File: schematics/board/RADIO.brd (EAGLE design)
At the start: 29 x 49 mm, 2 parts

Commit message: Платы подготовлены для Резонита
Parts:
- moved JP1 1.12 mm to (12.3, 47.5)
- moved RADIO 1.00 mm to (27.0, 5.23)
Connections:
- net N$1 renamed GND
- net N$2 renamed 5V
- net N$3 renamed AUX
- net N$4 renamed TXD
- net N$5 renamed RXD
- net N$6 renamed M1
- net N$7 renamed M0
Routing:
- net GND: track 79.7 -> 89.7 mm, vias 1 -> 0
- net RXD: track 22.8 -> 21.7 mm
- net M1: track 26.4 -> 25.3 mm
- net TXD: track 19.1 -> 18.1 mm
- net 5V: track 11.9 -> 10.9 mm
- net AUX: track 15.5 -> 14.5 mm
- net M0: track 29.8 -> 28.9 mm
- added copper zone on layer 1, net GND
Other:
- board size 29 x 49 mm -> 29 x 51 mm
- board text added: "5V"
- board text added: "AUX"
- board text added: "GND"
- board text added: "M0"
- board text added: "M1"
- board text added: "RX"
- board text added: "TX"

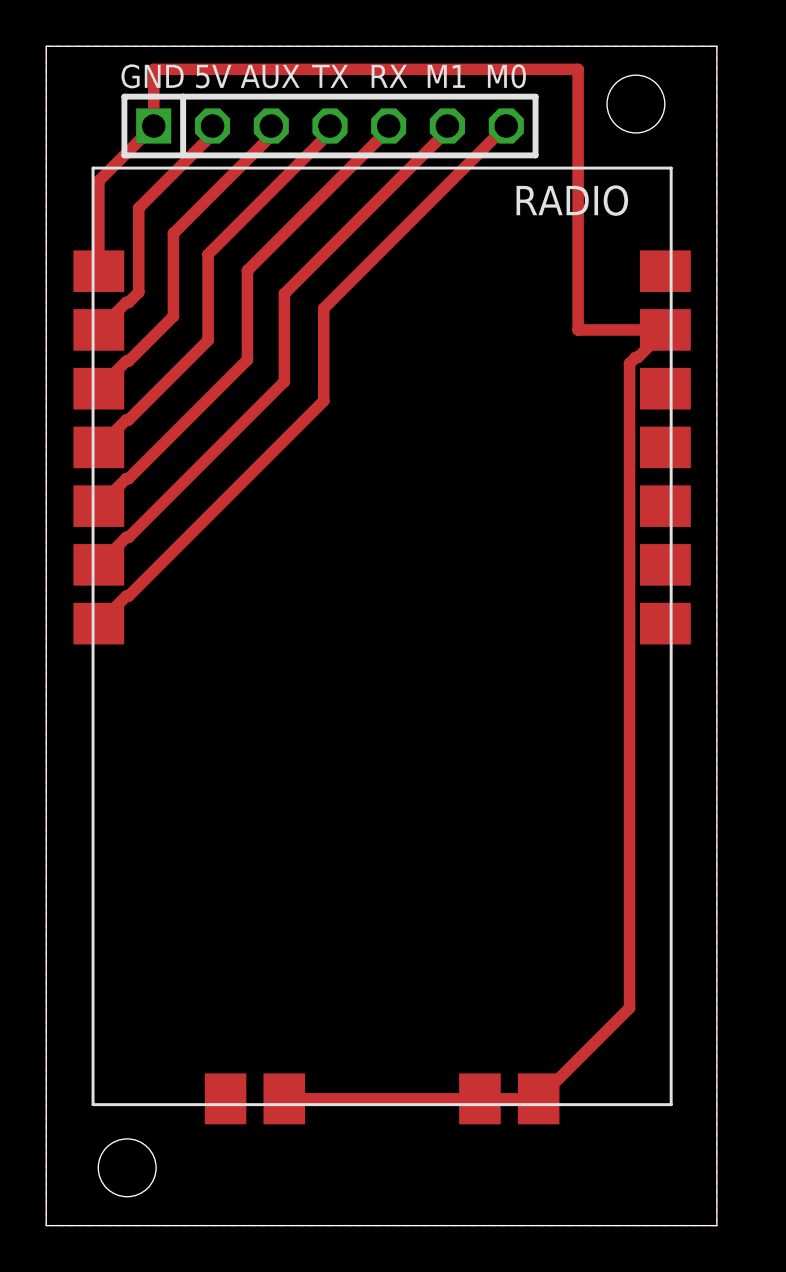
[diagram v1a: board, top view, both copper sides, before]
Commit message: GKS: допиливается конструкция, изменены размеры платы под радио
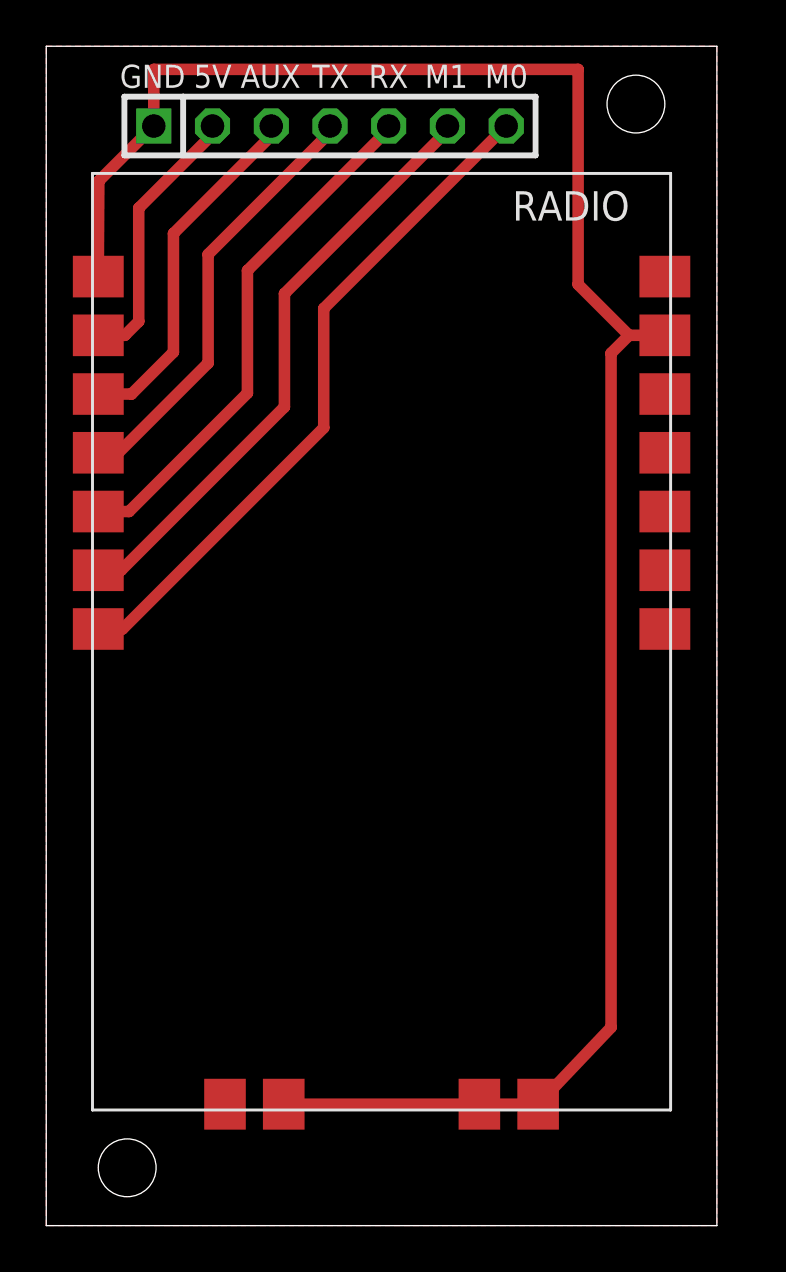
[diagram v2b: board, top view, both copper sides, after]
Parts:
- moved RADIO 0.23 mm to (27.0, 5.00)
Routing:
- net GND: track 89.7 -> 88.1 mm
- net AUX: track 14.5 -> 15.5 mm
- net RXD: track 21.7 -> 22.7 mm
- net 5V: track 10.9 -> 11.8 mm
- net M0: track 28.9 -> 29.7 mm
- net M1: track 25.3 -> 26.0 mm
- net TXD: track 18.1 -> 18.8 mm
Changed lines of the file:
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@@
 <?xml version="1.0" encoding="utf-8"?>
 <!DOCTYPE eagle SYSTEM "eagle.dtd">
-<eagle version="9.4.2">
+<eagle version="9.6.0">
 <drawing>
 <settings>
@@
 <attribute name="VALUE" x="3.38" y="44.375" size="1.27" layer="27"/>
 </element>
-<element name="RADIO" library="CanCubeSat" package="RADIO" value="RADIO" x="27.024" y="5.232" smashed="yes">
-<attribute name="NAME" x="20.184" y="43.692" size="1.27" layer="25"/>
+<element name="RADIO" library="CanCubeSat" package="RADIO" value="RADIO" x="27" y="5" smashed="yes">
+<attribute name="NAME" x="20.16" y="43.46" size="1.27" layer="25"/>
 </element>
 </elements>
@@
 <contactref element="RADIO" pad="P$17"/>
 <contactref element="JP1" pad="1"/>
-<wire x1="10.294" y1="5.482" x2="18.754" y2="5.482" width="0.5" layer="1"/>
-<wire x1="18.754" y1="5.482" x2="21.294" y2="5.482" width="0.5" layer="1"/>
-<wire x1="25.224" y1="37.27839375" x2="25.48760625" y2="37.542" width="0.5" layer="1"/>
-<wire x1="25.48760625" y1="37.542" x2="25.584" y2="37.542" width="0.5" layer="1"/>
-<wire x1="25.584" y1="37.542" x2="26.774" y2="38.732" width="0.5" layer="1"/>
-<wire x1="21.294" y1="5.482" x2="25.224" y2="9.412" width="0.5" layer="1"/>
-<wire x1="25.224" y1="9.412" x2="25.224" y2="37.27839375" width="0.5" layer="1"/>
-<wire x1="2.274" y1="41.272" x2="2.274" y2="45.174" width="0.5" layer="1"/>
+<wire x1="10.27" y1="5.25" x2="18.73" y2="5.25" width="0.5" layer="1"/>
+<wire x1="18.73" y1="5.25" x2="21.27" y2="5.25" width="0.5" layer="1"/>
+<wire x1="21.27" y1="5.25" x2="24.424" y2="8.569915625" width="0.5" layer="1"/>
+<wire x1="24.424" y1="37.724" x2="24.424" y2="8.569915625" width="0.5" layer="1"/>
+<wire x1="2.25" y1="41.04" x2="2.274" y2="45.174" width="0.5" layer="1"/>
 <wire x1="2.274" y1="45.174" x2="4.65" y2="47.55" width="0.5" layer="1"/>
 <polygon width="0.25" layer="1" isolate="0.5" thermals="no">
@@
 </polygon>
 <wire x1="4.65" y1="47.55" x2="4.65" y2="50" width="0.5" layer="1"/>
-<wire x1="23" y1="38.732" x2="26.774" y2="38.732" width="0.5" layer="1"/>
 <wire x1="4.65" y1="50" x2="23" y2="50" width="0.5" layer="1"/>
-<wire x1="23" y1="50" x2="23" y2="38.732" width="0.5" layer="1"/>
+<wire x1="23" y1="40.7" x2="23" y2="50" width="0.5" layer="1"/>
+<wire x1="26.75" y1="38.5" x2="25.2" y2="38.5" width="0.5" layer="1"/>
+<wire x1="25.2" y1="38.5" x2="23" y2="40.7" width="0.5" layer="1"/>
+<wire x1="24.424" y1="37.724" x2="25.2" y2="38.5" width="0.5" layer="1"/>
 </signal>
 <signal name="5V">
 <contactref element="RADIO" pad="P$6"/>
 <contactref element="JP1" pad="2"/>
-<wire x1="2.274" y1="38.732" x2="3.464" y2="39.922" width="0.5" layer="1"/>
-<wire x1="3.464" y1="39.922" x2="3.56039375" y2="39.922" width="0.5" layer="1"/>
-<wire x1="3.56039375" y1="39.922" x2="4" y2="40.36160625" width="0.5" layer="1"/>
-<wire x1="4" y1="40.36160625" x2="4" y2="44" width="0.5" layer="1"/>
 <wire x1="4" y1="44" x2="7.190015625" y2="47.190015625" width="0.5" layer="1"/>
 <wire x1="7.190015625" y1="47.190015625" x2="7.19" y2="47.55" width="0.5" layer="1"/>
+<wire x1="2.25" y1="38.5" x2="3.4" y2="38.5" width="0.5" layer="1"/>
+<wire x1="3.4" y1="38.5" x2="4" y2="39.1" width="0.5" layer="1"/>
+<wire x1="4" y1="39.1" x2="4" y2="44" width="0.5" layer="1"/>
 </signal>
 <signal name="AUX">
 <contactref element="RADIO" pad="P$5"/>
 <contactref element="JP1" pad="3"/>
-<wire x1="2.274" y1="36.192" x2="3.464" y2="37.382" width="0.5" layer="1"/>
-<wire x1="3.464" y1="37.382" x2="3.56039375" y2="37.382" width="0.5" layer="1"/>
-<wire x1="3.56039375" y1="37.382" x2="5.5" y2="39.32160625" width="0.5" layer="1"/>
-<wire x1="5.5" y1="39.32160625" x2="5.5" y2="42.9" width="0.5" layer="1"/>
 <wire x1="5.5" y1="42.9" x2="9.73" y2="47.13" width="0.5" layer="1"/>
 <wire x1="9.73" y1="47.13" x2="9.73" y2="47.55" width="0.5" layer="1"/>
+<wire x1="2.25" y1="35.96" x2="3.68844375" y2="35.96" width="0.5" layer="1"/>
+<wire x1="3.68844375" y1="35.96" x2="5.5" y2="37.77155625" width="0.5" layer="1"/>
+<wire x1="5.5" y1="37.77155625" x2="5.5" y2="42.9" width="0.5" layer="1"/>
 </signal>
 <signal name="TXD">
 <contactref element="RADIO" pad="P$4"/>
 <contactref element="JP1" pad="4"/>
-<wire x1="2.274" y1="33.652" x2="3.464" y2="34.842" width="0.5" layer="1"/>
-<wire x1="3.464" y1="34.842" x2="3.56039375" y2="34.842" width="0.5" layer="1"/>
-<wire x1="3.56039375" y1="34.842" x2="7" y2="38.28160625" width="0.5" layer="1"/>
-<wire x1="7" y1="38.28160625" x2="7" y2="42" width="0.5" layer="1"/>
 <wire x1="7" y1="42" x2="12.27" y2="47.27" width="0.5" layer="1"/>
 <wire x1="12.27" y1="47.27" x2="12.27" y2="47.55" width="0.5" layer="1"/>
+<wire x1="2.25" y1="33.42" x2="3.12" y2="33.42" width="0.5" layer="1"/>
+<wire x1="3.12" y1="33.42" x2="7" y2="37.3" width="0.5" layer="1"/>
+<wire x1="7" y1="37.3" x2="7" y2="42" width="0.5" layer="1"/>
 </signal>
 <signal name="RXD">
 <contactref element="RADIO" pad="P$3"/>
 <contactref element="JP1" pad="5"/>
-<wire x1="2.274" y1="31.112" x2="3.464" y2="32.302" width="0.5" layer="1"/>
-<wire x1="3.464" y1="32.302" x2="3.56039375" y2="32.302" width="0.5" layer="1"/>
-<wire x1="3.56039375" y1="32.302" x2="8.7" y2="37.44160625" width="0.5" layer="1"/>
-<wire x1="8.7" y1="37.44160625" x2="8.7" y2="41.3" width="0.5" layer="1"/>
 <wire x1="8.7" y1="41.3" x2="14.81" y2="47.41" width="0.5" layer="1"/>
 <wire x1="14.81" y1="47.41" x2="14.81" y2="47.55" width="0.5" layer="1"/>
+<wire x1="2.25" y1="30.88" x2="3.58" y2="30.88" width="0.5" layer="1"/>
+<wire x1="3.58" y1="30.88" x2="8.7" y2="36" width="0.5" layer="1"/>
+<wire x1="8.7" y1="36" x2="8.7" y2="41.3" width="0.5" layer="1"/>
 </signal>
 <signal name="M1">
 <contactref element="RADIO" pad="P$2"/>
 <contactref element="JP1" pad="6"/>
-<wire x1="2.274" y1="28.572" x2="3.464" y2="29.762" width="0.5" layer="1"/>
-<wire x1="3.464" y1="29.762" x2="3.56039375" y2="29.762" width="0.5" layer="1"/>
-<wire x1="3.56039375" y1="29.762" x2="10.3" y2="36.50160625" width="0.5" layer="1"/>
-<wire x1="10.3" y1="36.50160625" x2="10.3" y2="40.3" width="0.5" layer="1"/>
 <wire x1="10.3" y1="40.3" x2="17.35" y2="47.35" width="0.5" layer="1"/>
 <wire x1="17.35" y1="47.35" x2="17.35" y2="47.55" width="0.5" layer="1"/>
+<wire x1="2.25" y1="28.34" x2="3.24" y2="28.34" width="0.5" layer="1"/>
+<wire x1="3.24" y1="28.34" x2="10.3" y2="35.4" width="0.5" layer="1"/>
+<wire x1="10.3" y1="35.4" x2="10.3" y2="40.3" width="0.5" layer="1"/>
 </signal>
 <signal name="M0">
 <contactref element="RADIO" pad="P$1"/>
 <contactref element="JP1" pad="7"/>
-<wire x1="2.274" y1="26.032" x2="3.464" y2="27.222" width="0.5" layer="1"/>
-<wire x1="3.464" y1="27.222" x2="3.56039375" y2="27.222" width="0.5" layer="1"/>
-<wire x1="3.56039375" y1="27.222" x2="12" y2="35.66160625" width="0.5" layer="1"/>
 <wire x1="12" y1="39.66" x2="19.89" y2="47.55" width="0.5" layer="1"/>
-<wire x1="12" y1="35.66160625" x2="12" y2="39.66" width="0.5" layer="1"/>
+<wire x1="2.25" y1="25.8" x2="3.3" y2="25.8" width="0.5" layer="1"/>
+<wire x1="3.3" y1="25.8" x2="12" y2="34.5" width="0.5" layer="1"/>
+<wire x1="12" y1="34.5" x2="12" y2="39.66" width="0.5" layer="1"/>
 </signal>
 </signals>

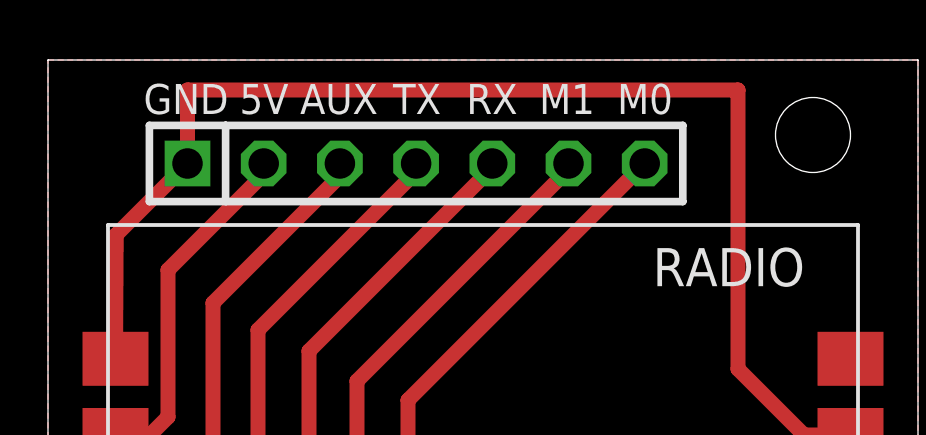
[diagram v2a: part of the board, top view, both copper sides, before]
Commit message: Добавлена схема АС, исправлена плата RADIO
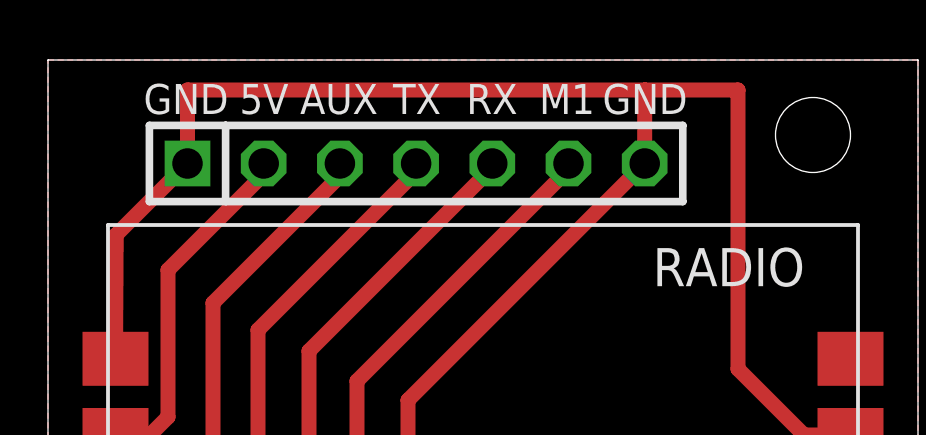
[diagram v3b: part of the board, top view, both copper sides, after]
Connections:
- removed net M0: JP1.7, RADIO.P$1
- net GND: now also JP1.7, RADIO.P$1
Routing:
- net GND: track 88.1 -> 120.2 mm
- net M0: track 29.7 -> 0.00 mm
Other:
- board text removed: "M0"
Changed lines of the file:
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@@
 <?xml version="1.0" encoding="utf-8"?>
 <!DOCTYPE eagle SYSTEM "eagle.dtd">
-<eagle version="9.6.0">
+<eagle version="9.4.2">
 <drawing>
 <settings>
@@
 <text x="14.8" y="49.2" size="1" layer="25" align="bottom-center">RX</text>
 <text x="17.3" y="49.2" size="1" layer="25" align="bottom-center">M1</text>
-<text x="19.9" y="49.2" size="1" layer="25" align="bottom-center">M0</text>
+<text x="19.9" y="49.2" size="1" layer="25" align="bottom-center">GND</text>
 </plain>
 <attributes>
@@
 </polygon>
 <wire x1="4.65" y1="47.55" x2="4.65" y2="50" width="0.5" layer="1"/>
-<wire x1="4.65" y1="50" x2="23" y2="50" width="0.5" layer="1"/>
+<wire x1="4.65" y1="50" x2="19.9" y2="50" width="0.5" layer="1"/>
+<wire x1="19.9" y1="50" x2="23" y2="50" width="0.5" layer="1"/>
 <wire x1="23" y1="40.7" x2="23" y2="50" width="0.5" layer="1"/>
 <wire x1="26.75" y1="38.5" x2="25.2" y2="38.5" width="0.5" layer="1"/>
 <wire x1="25.2" y1="38.5" x2="23" y2="40.7" width="0.5" layer="1"/>
 <wire x1="24.424" y1="37.724" x2="25.2" y2="38.5" width="0.5" layer="1"/>
+<contactref element="RADIO" pad="P$1"/>
+<contactref element="JP1" pad="7"/>
+<wire x1="12" y1="39.66" x2="19.89" y2="47.55" width="0.5" layer="1"/>
+<wire x1="2.25" y1="25.8" x2="3.3" y2="25.8" width="0.5" layer="1"/>
+<wire x1="3.3" y1="25.8" x2="12" y2="34.5" width="0.5" layer="1"/>
+<wire x1="12" y1="34.5" x2="12" y2="39.66" width="0.5" layer="1"/>
+<wire x1="19.89" y1="47.55" x2="19.89" y2="49.99" width="0.5" layer="1"/>
+<wire x1="19.89" y1="49.99" x2="19.9" y2="50" width="0.5" layer="1"/>
 </signal>
 <signal name="5V">
@@
 <wire x1="10.3" y1="35.4" x2="10.3" y2="40.3" width="0.5" layer="1"/>
 </signal>
-<signal name="M0">
-<contactref element="RADIO" pad="P$1"/>
-<contactref element="JP1" pad="7"/>
-<wire x1="12" y1="39.66" x2="19.89" y2="47.55" width="0.5" layer="1"/>
-<wire x1="2.25" y1="25.8" x2="3.3" y2="25.8" width="0.5" layer="1"/>
-<wire x1="3.3" y1="25.8" x2="12" y2="34.5" width="0.5" layer="1"/>
-<wire x1="12" y1="34.5" x2="12" y2="39.66" width="0.5" layer="1"/>
-</signal>
 </signals>

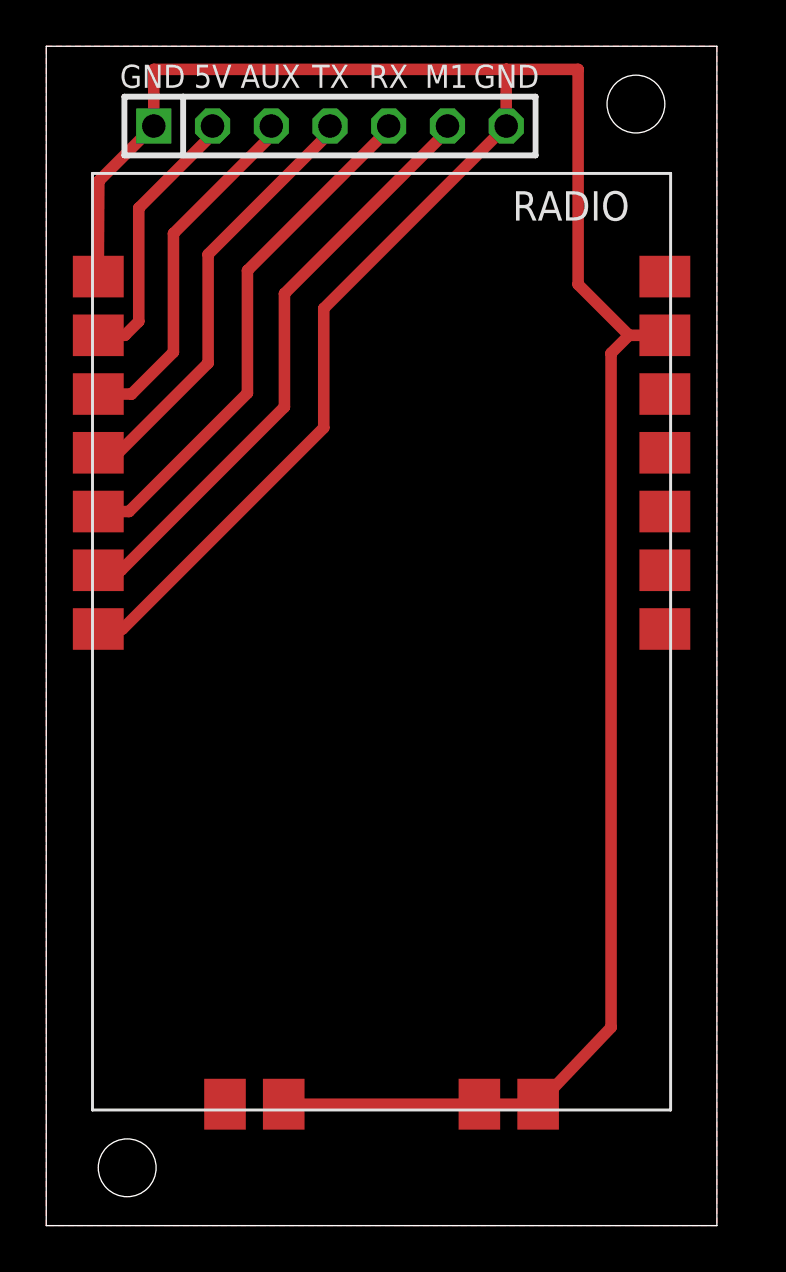
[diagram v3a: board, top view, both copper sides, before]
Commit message: Исправлены RADIO и диоды
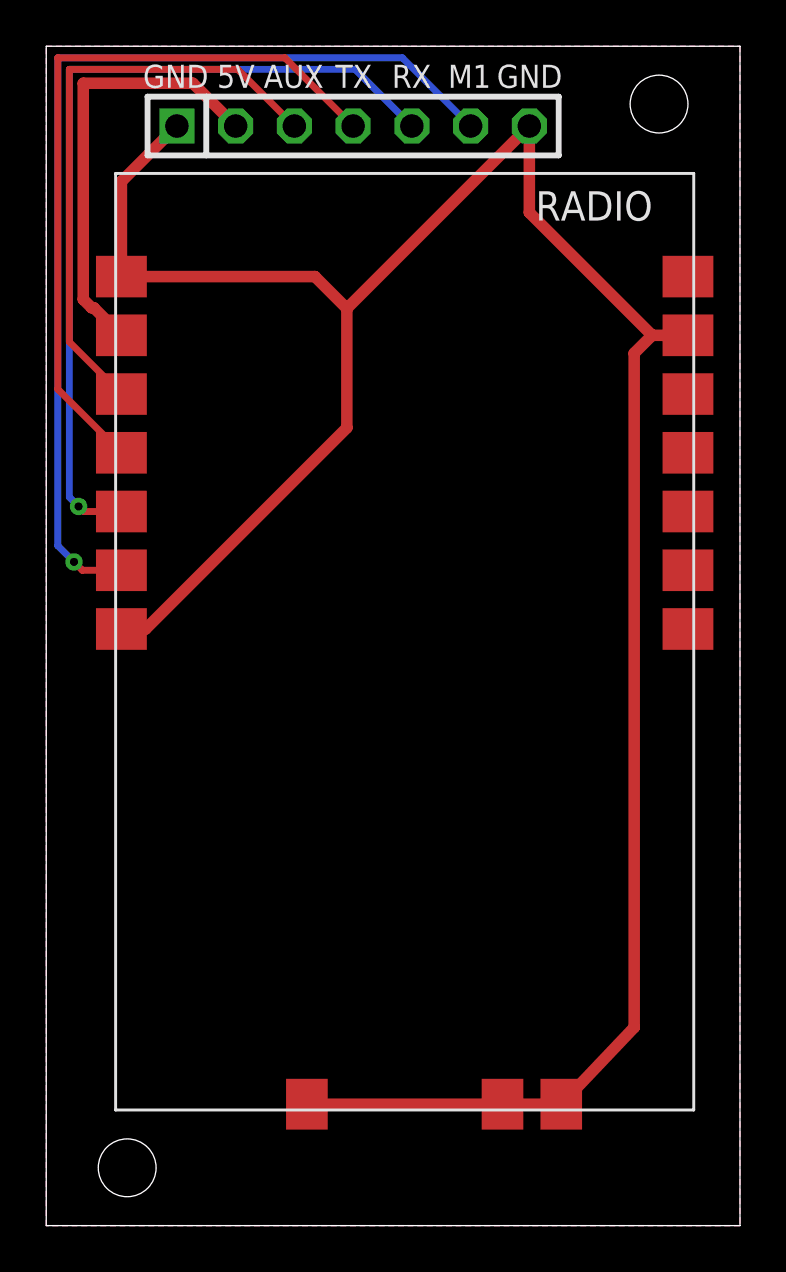
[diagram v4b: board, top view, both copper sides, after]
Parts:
- moved JP1 1.00 mm to (13.3, 47.5)
- moved RADIO 1.00 mm to (28.0, 5.00)
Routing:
- net M1: track 26.0 -> 43.4 mm, vias 0 -> 1
- net RXD: track 22.7 -> 36.8 mm, vias 0 -> 1
- net GND: track 120.2 -> 106.1 mm
- net TXD: track 18.8 -> 32.2 mm
- net AUX: track 15.5 -> 25.7 mm
- net 5V: track 11.8 -> 19.0 mm
- added copper zone on layer 16, net GND
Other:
- board size 29 x 51 mm -> 30 x 51 mm
